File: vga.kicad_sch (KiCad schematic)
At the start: 34 parts, among them J14 Component A/V, J17 Conn_01x03, J18 Conn_01x02, J19 Conn_01x03, J20 Conn_01x02, J21 Conn_01x03, J4 Conn_01x02

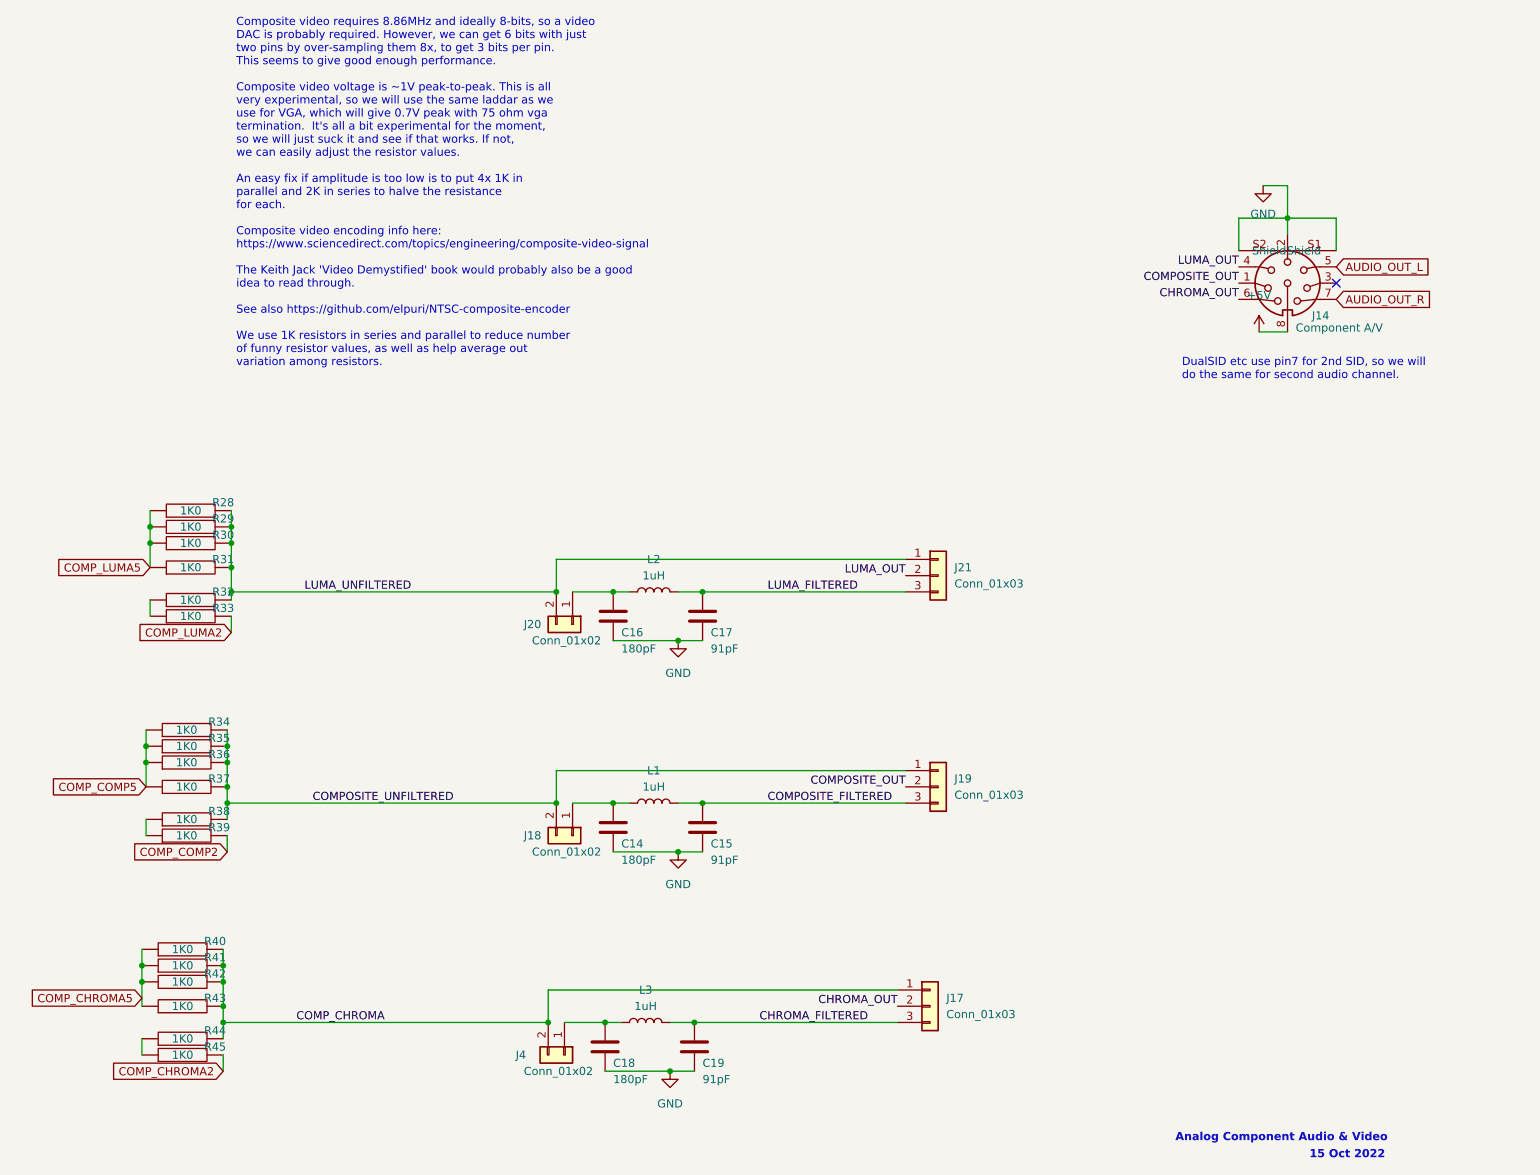
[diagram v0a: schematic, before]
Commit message: Remove everything not needed for JTAG loader board testing
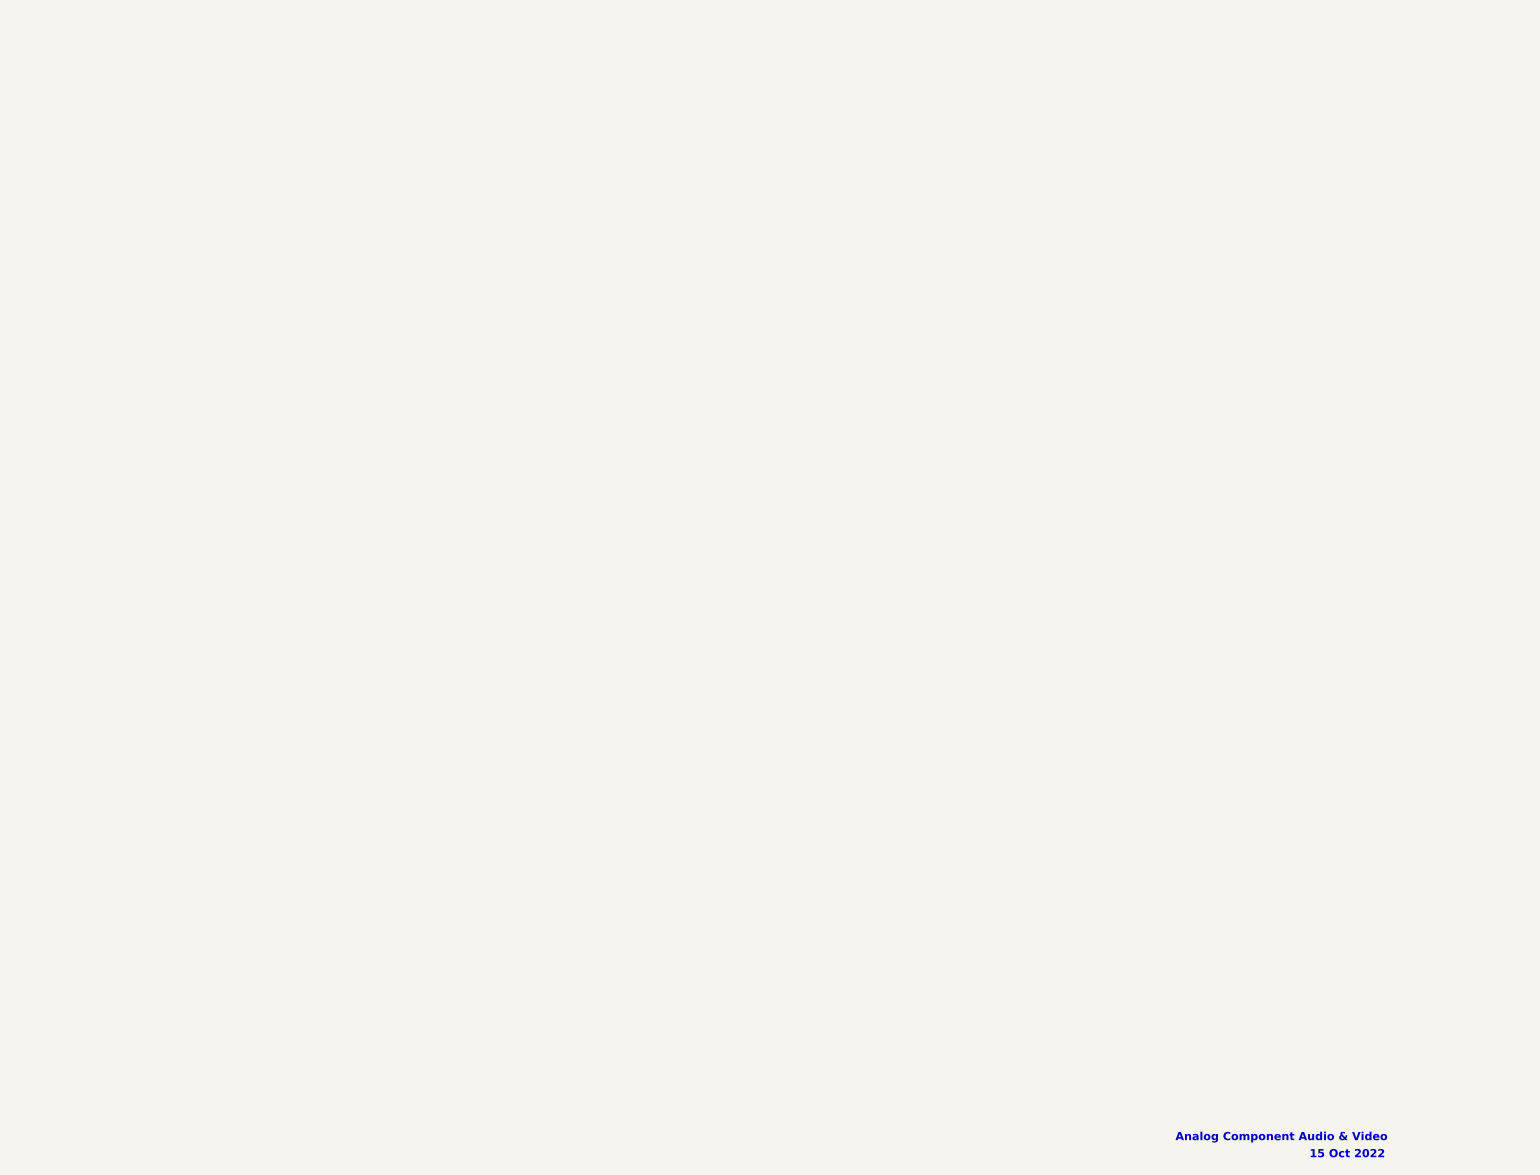
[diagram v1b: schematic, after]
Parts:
- removed C14, C16, C18: 180pF, Capacitor_THT:C_Disc_D5.0mm_W2.5mm_P5.00mm, symbol Device:C
- removed C15, C17, C19: 91pF, Capacitor_THT:C_Disc_D5.0mm_W2.5mm_P5.00mm, symbol Device:C
- removed J14: Component A/V, snapeda:CUI_SDF-80J, symbol 00Project-SDF-60J:SDF-80J
- removed J17, J19, J21: Conn_01x03, Connector_PinSocket_2.54mm:PinSocket_1x03_P2.54mm_Vertical, symbol Connector_Generic:Conn_01x03
- removed J18, J20, J4: Conn_01x02, Connector_PinSocket_2.54mm:PinSocket_1x02_P2.54mm_Vertical, symbol Connector_Generic:Conn_01x02
- removed L1, L2, L3: 1uH, Inductor_THT:L_Axial_L6.6mm_D2.7mm_P2.54mm_Vertical_Vishay_IM-2, symbol Device:L
- removed R28, R29, R30, R31, R32, R33, R34, R35, R36, R37, R38, R39, R40, R41, R42, R43, R44, R45: 1K0, snapeda:Labeled Resistor, symbol pspice:R
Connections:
- no-connect marks 1 -> 0
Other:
- note removed: "Composite video requires 8.86MHz and ideally 8-bits, so a video DAC is probably required. However, we can get 6 bits with just two pins by over-sampling them 8x, to get 3 bits per pin. This seems to give good enough performance. Composite video voltage is ~1V peak-to-peak. This is all very experimental, so we will use the same laddar as we use for VGA, which will give 0.7V peak with 75 ohm vga te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"
- note removed: "DualSID etc use pin7 for 2nd SID, so we will do the same for second audio channel."
